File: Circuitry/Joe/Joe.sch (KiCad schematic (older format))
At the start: 32 parts, among them J1 Conn_02x03_Counter_Clockwise, J2 Screw_Terminal_01x09, J3 USB_B_Micro, J4 Micro_SD_Card, U5 DS3231MZ, U6 UFDFPN8-MC, U7 DF12-20DS, U8 AP2127N-3.3, U9 ATmega32U4-MU

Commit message: burt organization and screw terminal and image sensor connector
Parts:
- removed J2: Screw_Terminal_01x09, symbol Connector:Screw_Terminal_01x09
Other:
- note added: "CS Output for Img Sensor"
- note added: "MISO Output for Img Sensor"
- note added: "MOSI Output for Img Sensor"
- note added: "Motor Driver for Launchers Output 1"
- note added: "Motor Driver for Launchers Output 2\n"
- note added: "Reg Clk Output for Shift Reg"
- note added: "SCL Output for Img Sensor"
- note added: "SCLK Output for Img Sensor"
- note added: "SDA Output for Img Sensor"
- note added: "Serial Clk Output for Shift Reg"
- note added: "Serial Output for Shift Reg"
- note removed: "RX Output for Img Processor"
- note removed: "Reg Clk Output for Shift Regs\n"
- note removed: "Serial Clk Output for Shift Regs\n"
- note removed: "Serial Output for Shift Regs"
- note removed: "TX Output for Img Processor"
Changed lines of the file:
@@
 Wire Notes Line
 	6200 500  4050 500
-Text Label 4525 3350 2    50   ~ 0
+Text Label 4525 3800 2    50   ~ 0
 BP1
-Text Label 4525 3450 2    50   ~ 0
+Text Label 4525 3900 2    50   ~ 0
 BP2
 $Comp
@@
 $EndComp
 Text Label 4525 3150 2    50   ~ 0
-TX
+CS
 Text Label 4525 3250 2    50   ~ 0
-RX
-Text Label 4525 3550 2    50   ~ 0
+MOSI
+Text Label 4525 4000 2    50   ~ 0
 SER
-Text Label 4525 3650 2    50   ~ 0
+Text Label 4525 4100 2    50   ~ 0
 SRCLK
-Text Label 4525 3750 2    50   ~ 0
+Text Label 4525 4200 2    50   ~ 0
 RCLK
 $Comp
@@
 Img Sensor Data Input
 Text Notes 4950 3150 0    39   ~ 0
-TX Output for Img Processor
+CS Output for Img Sensor
 Text Notes 4950 3250 0    39   ~ 0
-RX Output for Img Processor
-Text Notes 4950 3350 0    39   ~ 0
+MOSI Output for Img Sensor
+Text Notes 4950 3800 0    39   ~ 0
 Burn Wire Output 1 for Pyrolysis
-Text Notes 4950 3450 0    39   ~ 0
+Text Notes 4950 3900 0    39   ~ 0
 Burn Wire Output 2 for Pyrolysis
-Text Notes 4950 3550 0    39   ~ 0
-Serial Output for Shift Regs
-Text Notes 4950 3650 0    39   ~ 0
-Serial Clk Output for Shift Regs\n
-Text Notes 4950 3750 0    39   ~ 0
-Reg Clk Output for Shift Regs\n
+Text Notes 4950 4000 0    39   ~ 0
+Serial Output for Shift Reg
+Text Notes 4950 4200 0    39   ~ 0
+Reg Clk Output for Shift Reg
 Text Notes 4350 2775 0    39   ~ 0
 Input = Data from Burt to Joe\nOutput = Data from Joe to Burt
-$Comp
-L Connector:Screw_Terminal_01x09 J2
-U 1 1 5D2DF900
-P 4725 3350
-F 0 "J2" H 5300 4100 50  0000 L CNN
-F 1 "Screw_Terminal_01x09" H 4350 4100 50  0000 L CNN
-F 2 "" H 4725 3350 50  0001 C CNN
-F 3 "~" H 4725 3350 50  0001 C CNN
-F 4 "https://www.digikey.com/product-detail/en/amphenol-anytek/VI0921550000G/609-3943-ND/2261377" H 4725 3350 50  0001 C CNN "Part URL"
-	1    4725 3350
-	1    0    0    -1
-$EndComp
 Wire Notes Line
 	4200 2475 6200 2475
 Wire Notes Line
 	6200 2475 6200 3825
-Wire Notes Line
-	6200 3825 4200 3825
 Wire Notes Line
 	4200 3825 4200 2475
@@
 Wire Wire Line
 	1900 6950 2225 6950
+Text Label 4525 4300 2    50   ~ 0
+IN1
+Text Label 4525 4400 2    50   ~ 0
+IN2
+Text Notes 4950 4300 0    39   ~ 0
+Motor Driver for Launchers Output 1
+Text Notes 4950 4400 0    39   ~ 0
+Motor Driver for Launchers Output 2\n
+Text Notes 4950 4100 0    39   ~ 0
+Serial Clk Output for Shift Reg
+Text Label 4525 3350 2    50   ~ 0
+MISO
+Text Label 4525 3450 2    50   ~ 0
+SCLK
+Text Label 4525 3550 2    50   ~ 0
+SDA
+Text Label 4525 3650 2    50   ~ 0
+SCL
+Text Notes 4950 3350 0    39   ~ 0
+MISO Output for Img Sensor
+Text Notes 4950 3450 0    39   ~ 0
+SCLK Output for Img Sensor
+Text Notes 4950 3550 0    39   ~ 0
+SDA Output for Img Sensor
+Text Notes 4950 3650 0    39   ~ 0
+SCL Output for Img Sensor
 $EndSCHEMATC

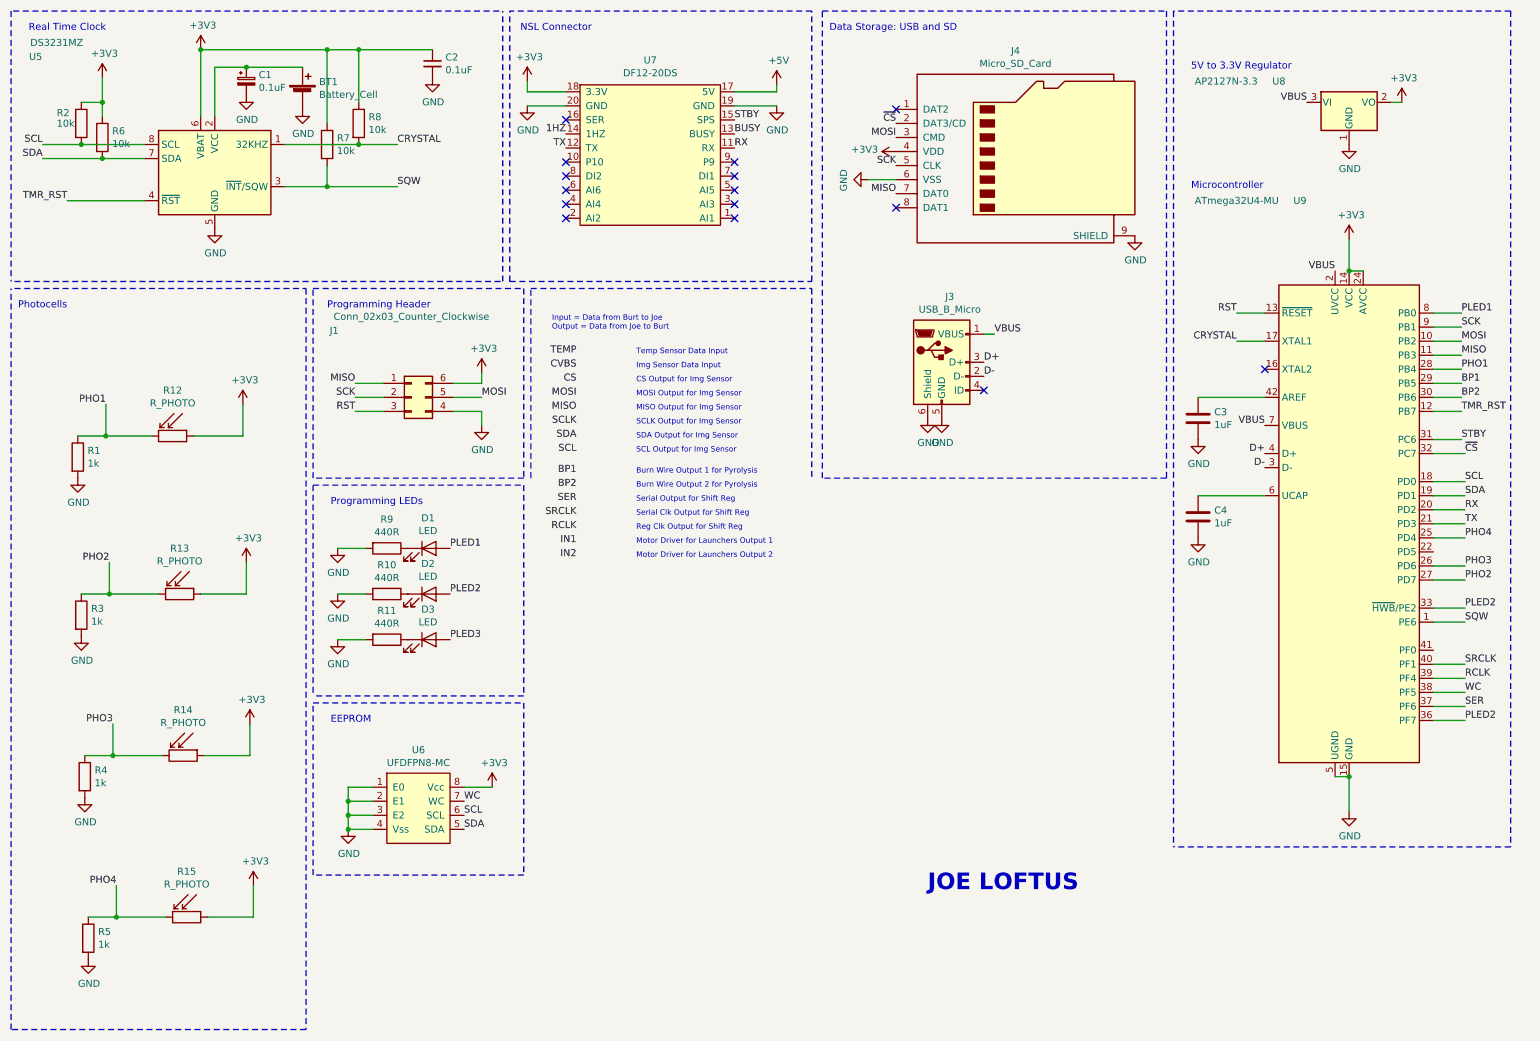
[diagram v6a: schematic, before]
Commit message: Added custom footprint library
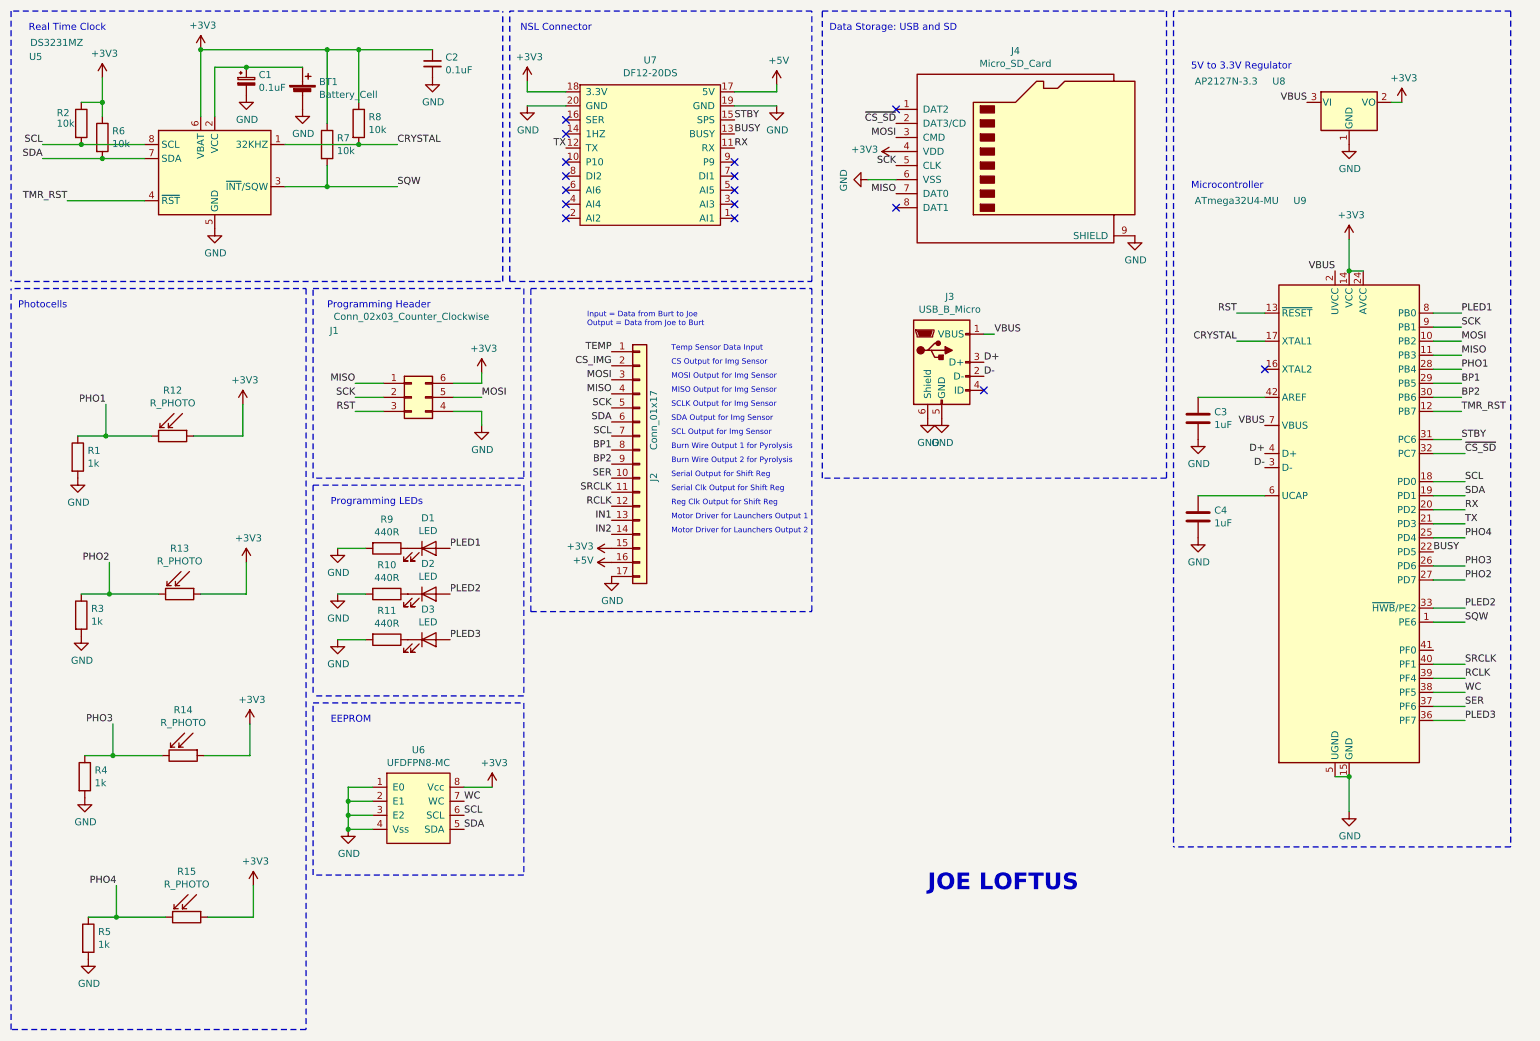
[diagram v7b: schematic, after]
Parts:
- added J2: Conn_01x17, symbol Connector_Generic:Conn_01x17
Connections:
- net +3V3: now also J2.15 (Pin_15)
- net +5V: now also J2.16 (Pin_16)
- net BP1: now also J2.8 (Pin_8)
- net BP2: now also J2.9 (Pin_9)
- net BUSY: now also U9.22 (PD5)
- net GND: now also J2.17 (Pin_17)
- net IN1: now also J2.13 (Pin_13)
- net IN2: now also J2.14 (Pin_14)
- net MISO: now also J2.4 (Pin_4)
- net MOSI: now also J2.3 (Pin_3)
- net PLED2: no longer U9.36 (PF7)
- net PLED3: now also U9.36 (PF7)
- net RCLK: now also J2.12 (Pin_12)
- net SCK: now also J2.5 (Pin_5)
- net SCL: now also J2.7 (Pin_7)
- net SDA: now also J2.6 (Pin_6)
- net SER: now also J2.10 (Pin_10)
- net SRCLK: now also J2.11 (Pin_11)
- net TEMP: now also J2.1 (Pin_1)
- net 1HZ: no longer names the net of U7.14 (1HZ)
- net ~CS renamed ~CS_SD
- new net CS_IMG: J2.2 (Pin_2)
- no-connect marks 15 -> 16
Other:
- note removed: "Img Sensor Data Input"
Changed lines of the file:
@@
 Text Label 10850 4250 0    50   ~ 0
 PHO4
-Text Label 4525 2950 2    50   ~ 0
+Text Label 4775 2925 2    50   ~ 0
 TEMP
 Wire Wire Line
@@
 Wire Wire Line
 	900  1850 1450 1850
-Text Label 4450 1375 2    50   ~ 0
-1HZ
 Wire Wire Line
 	1150 1150 1150 975
@@
 Wire Wire Line
 	10625 3550 10825 3550
-Text Label 4525 3050 2    50   ~ 0
-CVBS
 Wire Wire Line
 	3725 6025 3925 6025
@@
 Wire Notes Line
 	6200 500  4050 500
-Text Label 4525 3800 2    50   ~ 0
+Text Label 4775 3625 2    50   ~ 0
 BP1
-Text Label 4525 3900 2    50   ~ 0
+Text Label 4775 3725 2    50   ~ 0
 BP2
 $Comp
@@
 MOSI
 Text Label 6800 1300 2    50   ~ 0
-~CS
+~CS_SD
 Text Label 6800 1600 2    50   ~ 0
 SCK
@@
 NoConn ~ 6800 1200
 Text Label 10850 3650 0    50   ~ 0
-~CS
+~CS_SD
 Wire Wire Line
 	10625 3650 10850 3650
@@
 	1    0    0    -1
 $EndComp
-Text Label 4525 3150 2    50   ~ 0
-CS
-Text Label 4525 3250 2    50   ~ 0
+Text Label 4775 3025 2    50   ~ 0
+CS_IMG
+Text Label 4775 3125 2    50   ~ 0
 MOSI
-Text Label 4525 4000 2    50   ~ 0
+Text Label 4775 3825 2    50   ~ 0
 SER
-Text Label 4525 4100 2    50   ~ 0
+Text Label 4775 3925 2    50   ~ 0
 SRCLK
-Text Label 4525 4200 2    50   ~ 0
+Text Label 4775 4025 2    50   ~ 0
 RCLK
 $Comp
@@
 	1    0    0    -1
 $EndComp
-Text Notes 4950 2950 0    39   ~ 0
+Text Notes 5200 2925 0    39   ~ 0
 Temp Sensor Data Input
-Text Notes 4950 3050 0    39   ~ 0
-Img Sensor Data Input
-Text Notes 4950 3150 0    39   ~ 0
+Text Notes 5200 3025 0    39   ~ 0
 CS Output for Img Sensor
-Text Notes 4950 3250 0    39   ~ 0
+Text Notes 5200 3125 0    39   ~ 0
 MOSI Output for Img Sensor
-Text Notes 4950 3800 0    39   ~ 0
+Text Notes 5200 3625 0    39   ~ 0
 Burn Wire Output 1 for Pyrolysis
-Text Notes 4950 3900 0    39   ~ 0
+Text Notes 5200 3725 0    39   ~ 0
 Burn Wire Output 2 for Pyrolysis
-Text Notes 4950 4000 0    39   ~ 0
+Text Notes 5200 3825 0    39   ~ 0
 Serial Output for Shift Reg
-Text Notes 4950 4200 0    39   ~ 0
+Text Notes 5200 4025 0    39   ~ 0
 Reg Clk Output for Shift Reg
-Text Notes 4350 2775 0    39   ~ 0
+Text Notes 4600 2750 0    39   ~ 0
 Input = Data from Burt to Joe\nOutput = Data from Joe to Burt
 Wire Notes Line
 	4200 2475 6200 2475
 Wire Notes Line
-	6200 2475 6200 3825
-Wire Notes Line
-	4200 3825 4200 2475
+	6200 2475 6200 4775
+Wire Notes Line
+	4200 4775 4200 2475
 Wire Notes Line
 	2650 5425 4150 5425
@@
 	10625 4750 10850 4750
 Text Label 10850 5550 0    50   ~ 0
-PLED2
+PLED3
 Wire Wire Line
 	10625 5550 10850 5550
@@
 Wire Wire Line
 	1900 6950 2225 6950
-Text Label 4525 4300 2    50   ~ 0
+Text Label 4775 4125 2    50   ~ 0
 IN1
-Text Label 4525 4400 2    50   ~ 0
+Text Label 4775 4225 2    50   ~ 0
 IN2
-Text Notes 4950 4300 0    39   ~ 0
+Text Notes 5200 4125 0    39   ~ 0
 Motor Driver for Launchers Output 1
-Text Notes 4950 4400 0    39   ~ 0
+Text Notes 5200 4225 0    39   ~ 0
 Motor Driver for Launchers Output 2\n
-Text Notes 4950 4100 0    39   ~ 0
+Text Notes 5200 3925 0    39   ~ 0
 Serial Clk Output for Shift Reg
-Text Label 4525 3350 2    50   ~ 0
+Text Label 4775 3225 2    50   ~ 0
 MISO
-Text Label 4525 3450 2    50   ~ 0
-SCLK
-Text Label 4525 3550 2    50   ~ 0
+Text Label 4775 3325 2    50   ~ 0
+SCK
+Text Label 4775 3425 2    50   ~ 0
 SDA
-Text Label 4525 3650 2    50   ~ 0
+Text Label 4775 3525 2    50   ~ 0
 SCL
-Text Notes 4950 3350 0    39   ~ 0
+Text Notes 5200 3225 0    39   ~ 0
 MISO Output for Img Sensor
-Text Notes 4950 3450 0    39   ~ 0
+Text Notes 5200 3325 0    39   ~ 0
 SCLK Output for Img Sensor
-Text Notes 4950 3550 0    39   ~ 0
+Text Notes 5200 3425 0    39   ~ 0
 SDA Output for Img Sensor
-Text Notes 4950 3650 0    39   ~ 0
+Text Notes 5200 3525 0    39   ~ 0
 SCL Output for Img Sensor
+$Comp
+L power:+3V3 #PWR037
+U 1 1 5D47F25B
+P 4775 4325
+F 0 "#PWR037" H 4775 4175 50  0001 C CNN
+F 1 "+3V3" V 4790 4453 50  0000 L CNN
+F 2 "" H 4775 4325 50  0001 C CNN
+F 3 "" H 4775 4325 50  0001 C CNN
+	1    4775 4325
+	0    -1   -1   0
+$EndComp
+$Comp
+L power:+5V #PWR038
+U 1 1 5D480338
+P 4775 4425
+F 0 "#PWR038" H 4775 4275 50  0001 C CNN
+F 1 "+5V" V 4790 4553 50  0000 L CNN
+F 2 "" H 4775 4425 50  0001 C CNN
+F 3 "" H 4775 4425 50  0001 C CNN
+	1    4775 4425
+	0    -1   -1   0
+$EndComp
+$Comp
+L power:GND #PWR039
+U 1 1 5D480BD6
+P 4775 4525
+F 0 "#PWR039" H 4775 4275 50  0001 C CNN
+F 1 "GND" H 4780 4352 50  0000 C CNN
+F 2 "" H 4775 4525 50  0001 C CNN
+F 3 "" H 4775 4525 50  0001 C CNN
+	1    4775 4525
+	1    0    0    -1
+$EndComp
+Text Label 10625 4350 0    50   ~ 0
+BUSY
+NoConn ~ 4450 1375
+$Comp
+L Connector_Generic:Conn_01x17 J2
+U 1 1 5D48D629
+P 4975 3725
+F 0 "J2" V 5075 3600 50  0000 L CNN
+F 1 "Conn_01x17" V 5075 3825 50  0000 L CNN
+F 2 "" H 4975 3725 50  0001 C CNN
+F 3 "~" H 4975 3725 50  0001 C CNN
+F 4 "https://www.digikey.com/product-detail/en/molex/0522071733/WM10952CT-ND/5170967" H 4975 3725 50  0001 C CNN "Part URL"
+	1    4975 3725
+	1    0    0    -1
+$EndComp
+Wire Notes Line
+	4200 4775 6200 4775
 $EndSCHEMATC

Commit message: Got footprints for Cosmic DC
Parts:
- BT1: footprint (none) -> Battery:BatteryHolder_Keystone_3034_1x20mm
- C1, C2, C3, C4: footprint (none) -> Capacitor_SMD:C_0603_1608Metric
- D1, D2, D3: footprint (none) -> LED_SMD:LED_0603_1608Metric
- J1: footprint (none) -> Connector_PinHeader_2.54mm:PinHeader_2x03_P2.54mm_Vertical
- J2: footprint (none) -> Custom:0522071733
- J3: footprint (none) -> Connector_USB:USB_Micro-B_Molex-105017-0001; Part URL https://www.digikey.com/product-detail/en/amphenol-icc-fci/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 -> https://www.digikey.com/product-detail/en/molex/1050170001/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
- J4: footprint (none) -> Connector_Card:microSD_HC_Wuerth_693072010801; Part URL https://www.digikey.com/product-detail/en/molex/1051620001/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 -> https://www.digikey.com/product-detail/en/wurth-electronics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
- R1, R10, R11, R2, R3, R4, R5, R6, R7, R8, R9: footprint (none) -> Resistor_SMD:R_0603_1608Metric
- R12, R13, R14, R15: footprint (none) -> OptoDevice:R_LDR_10x8.5mm_P7.6mm_Vertical
- U6: value UFDFPN8-MC -> M24C32-XDW5TP; footprint (none) -> Package_SO:TSSOP-8_4.4x3mm_P0.65mm; Part URL https://www.digikey.com/products/en/integrated-circuits-ics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 -> https://www.digikey.com/product-detail/en/stmicroelectronic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
- U7: footprint (none) -> Custom:DF12-20DS-0.5V(86)
